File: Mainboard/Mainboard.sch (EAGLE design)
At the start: 9 parts, among them J1 USB3076-XX-X_REVC, J2 640455-5, J3 640455-2, J4 640455-4, J5 640455-4, J6 SJ-3523-SMT-TR, J7 640455-2, J8 929850-01-06-RB

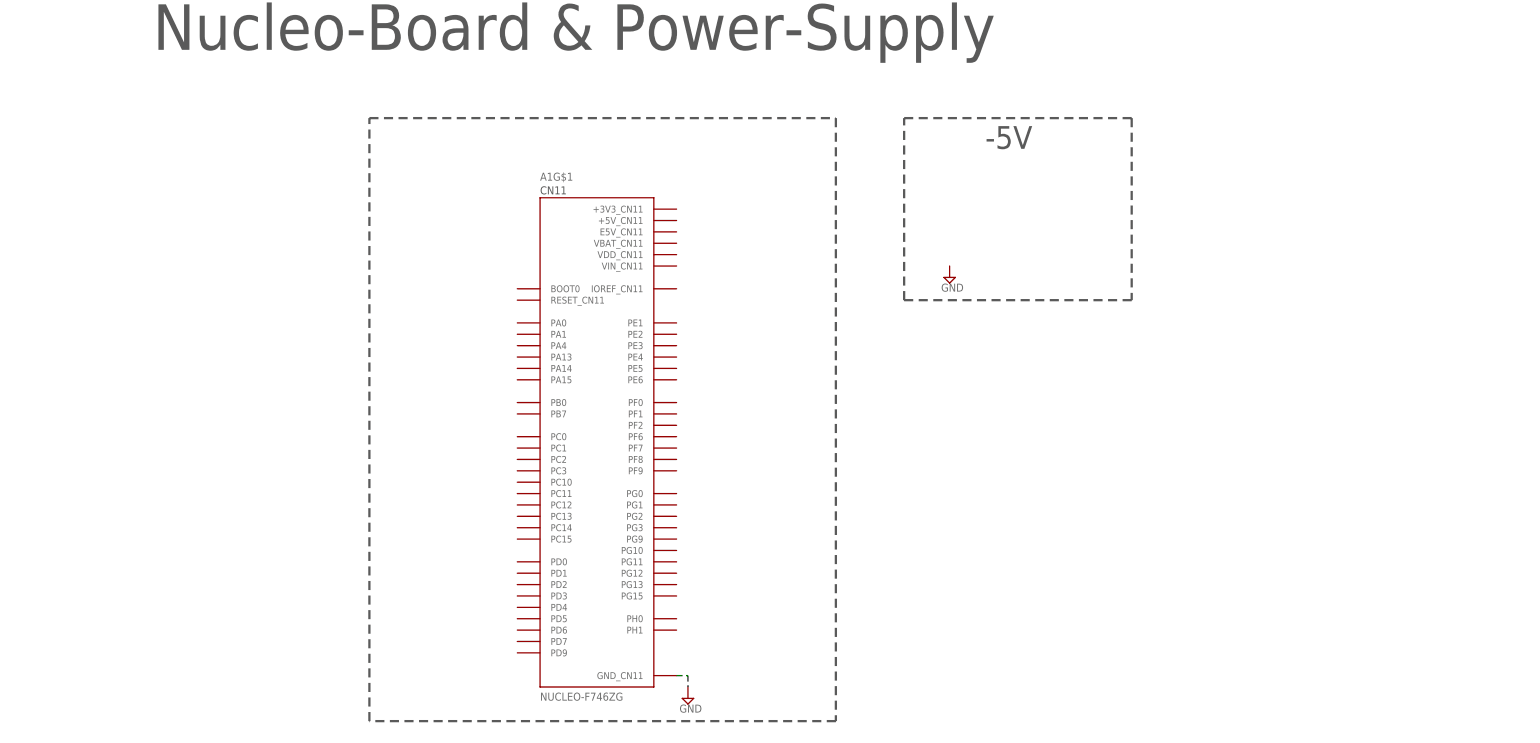
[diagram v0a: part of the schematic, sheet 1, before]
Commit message: Mainboard updated
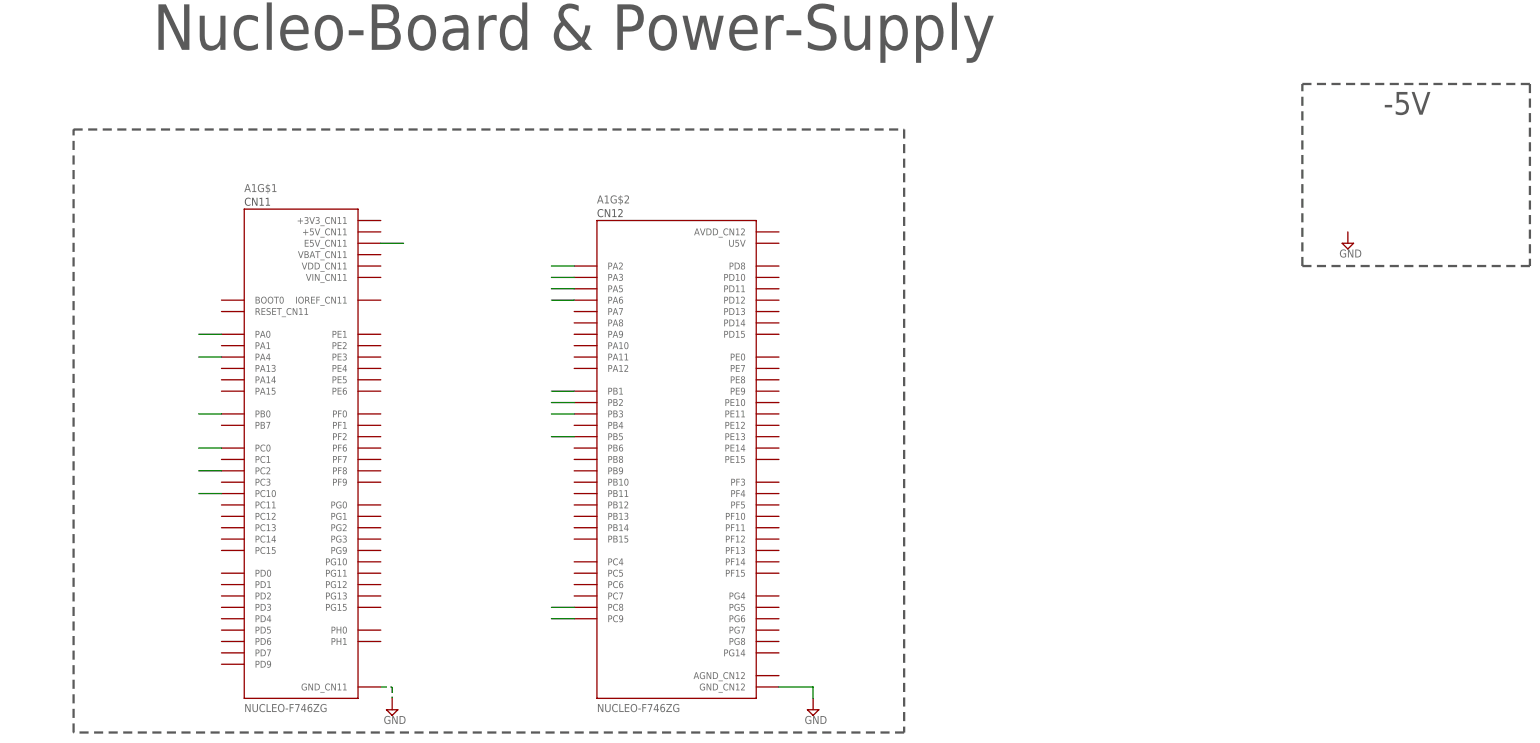
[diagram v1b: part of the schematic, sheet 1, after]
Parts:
- added C1, C2: 100n, rcl:C-EUC0603
- added C3, C4: 1u, rcl:C-EUC0603
- added IC1: TL072CD, SamacSys_Parts:TL072CD
- added IC2: LM386M-1_NOPB, SamacSys_Parts:LM386M-1_NOPB
- added J9: 61201421721, 61201421721:61201421721
- added R1, R9: 10k, rcl:R-EU_R0603
- added R10, R2, R3: 0, rcl:R-EU_R0603
- added R4: NP_0, rcl:R-EU_R0603
- added R5: 4k7, rcl:R-EU_R0603
- added R6: 15k, rcl:R-EU_R0603
- added R7: 33k, rcl:R-EU_R0603
- added R8: 100, rcl:R-EU_R0603
- added TS53YL104MR10: 100k, SamacSys_Parts:TS53YL203MR10
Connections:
- new net +3V3: J9.8
- new net 1_IN+: C3.2, IC1.1IN+, R1.2, R5.1
- new net 1_IN-: IC1.1IN-, R2.1
- new net 1_OUT: C3.1, IC1.1OUT, R3.1
- new net 2_IN-: IC1.2IN-, R6.2, R7.1
- new net 2_OUT: IC1.2OUT, R7.2, R8.1
- new net ADC_POTI: J9.9
- new net BUTTON_BACK: J9.13
- new net BUTTON_ENTER: J9.14
- new net DAC_OUT1: R10.1
- new net DISP_BUSY: J9.1
- new net DISP_CLK: J9.5
- new net DISP_CS: J9.4
- new net DISP_DC: J9.3
- new net DISP_DIN: J9.6
- new net DISP_RST: J9.2
- new net JOYSTICK_SW: J9.10
- new net JOYSTICK_VRX: J9.11
- new net JOYSTICK_VRY: J9.12
- new net N$1: A1G$1.E5V_CN11
- new net N$10: A1G$2.PB2
- new net N$11: A1G$2.PB3
- new net N$12: A1G$2.PB5
- new net N$13: A1G$1.PC0
- new net N$14: A1G$1.PC2
- new net N$15: A1G$2.PC8
- new net N$16: A1G$2.PC9
- new net N$17: A1G$1.PC10
- new net N$18: R10.2
- new net N$19: R2.2, R3.2, R4.1
- new net N$2: A1G$1.PA0
- new net N$20: R5.2, TS53YL104MR10.A
- new net N$21: R6.1, TS53YL104MR10.B
- new net N$22: C4.1, R8.2
- new net N$3: A1G$2.PA2
- new net N$4: A1G$2.PA3
- new net N$5: A1G$1.PA4
- new net N$6: A1G$2.PA5
- new net N$7: A1G$2.PA6
- new net N$8: A1G$1.PB0
- new net N$9: A1G$2.PB1
- net +5V: now also C2.2, IC1.VCC+
- net -5V: now also C1.2, IC1.VCC-
- net GND: now also A1G$2.GND_CN12, C1.1, C2.1, IC1.2IN+, J9.7, R1.1, R4.2, R9.1, TS53YL104MR10.C
- net PREAMP_AUDIO_OUT: now also C4.2, R9.2
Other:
- note added: "Adjustable Low Noise Preamplifier"
- note added: "Buffer / Non-Inverting Amp & Low Noise Preamplifier (for Headphones)"
- note added: "Buffer / Noninverting Amp."
- note added: "Highpass (DC-Filtering @ 16Hz)"
- note added: "IC Symbol & Power Supply Buffering"
- moved on the sheet: A1G$1

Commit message: Mainboard updated II
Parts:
- added C10, C7: 1m, rcl:CPOL-EUE2.5-5
- added C11: 1u, rcl:C-EUC0603
- added C5, C6: 100u, rcl:CPOL-EUE2.5-5
- added C8: 100n, rcl:C-EUC0603
- added C9: NP_10u, rcl:C-EUC0603
- added R11: NP_1k2, rcl:R-EU_R0603
- added R12, R13: 0, rcl:R-EU_R0603
- added R14: 10k, rcl:R-EU_R0603
- added TS53YL104MR1: 10k, SamacSys_Parts:TS53YL203MR10
- J3: value 640455-2 -> 640455-3; device 640455-2:640455-2 -> 640455-3:640455-3
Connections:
- net N$3 renamed USART2_TX
- net N$4 renamed USART2_RX
- removed net N$10: A1G$2.PB2
- removed net N$11: A1G$2.PB3
- removed net N$12: A1G$2.PB5
- removed net N$13: A1G$1.PC0
- removed net N$14: A1G$1.PC2
- removed net N$15: A1G$2.PC8
- removed net N$16: A1G$2.PC9
- removed net N$17: A1G$1.PC10
- removed net N$2: A1G$1.PA0
- removed net N$5: A1G$1.PA4
- removed net N$6: A1G$2.PA5
- removed net N$7: A1G$2.PA6
- removed net N$8: A1G$1.PB0
- removed net N$9: A1G$2.PB1
- new net ADC_EMG_AC: A1G$1.PF7
- new net ADC_EMG_DC: A1G$1.PF6
- new net ADC_KEYS: A1G$1.PC2, C11.1, R14.2
- new net DAC_OUT2: A1G$2.PA5, R13.1
- new net GYRO_I2C_SCL: A1G$1.PF1
- new net GYRO_I2C_SDA: A1G$1.PF0
- new net N$23: IC2.GAIN_1, R11.1
- new net N$24: IC2.+INPUT, TS53YL104MR1.B
- new net N$25: C9.1, R11.2
- new net N$26: C9.2, IC2.GAIN_2
- new net N$27: R12.2, TS53YL104MR1.A
- new net N$28: C5.+, IC2.BYPASS
- new net N$29: C7.+, C8.1, IC2.VOUT
- new net USART3_RX: A1G$1.PD9
- new net USART3_TX: A1G$2.PD8
- net +5V: now also A1G$1.E5V_CN11, C10.+, C6.+, IC2.VS
- net 1_OUT: now also R12.1
- net ADC_POTI: now also A1G$1.PC0
- net BUTTON_BACK: now also A1G$2.PC9
- net BUTTON_ENTER: now also A1G$2.PE8
- net DAC_OUT1: now also A1G$1.PA4
- net DISP_BUSY: now also A1G$2.PB1
- net DISP_CLK: now also A1G$2.PB3
- net DISP_CS: now also A1G$2.PC8
- net DISP_DC: now also A1G$1.PA0
- net DISP_DIN: now also A1G$2.PB5
- net DISP_RST: now also A1G$2.PF12
- net GND: now also C10.-, C11.2, C5.-, C6.-, C8.2, IC2.-INPUT, IC2.GND, TS53YL104MR1.C
- net JOYSTICK_SW: now also A1G$1.PG0
- net JOYSTICK_VRX: now also A1G$2.PA6
- net JOYSTICK_VRY: now also A1G$1.PB0
- net N$1: now also J3.3, R14.1; no longer A1G$1.E5V_CN11
- net N$18: now also R13.2
- net POWERAMP_AUDIO_OUT: now also C7.-
- net SD_CLK: now also A1G$1.PC10
- net SD_CS: now also A1G$2.PF10
- net SD_DI: now also A1G$2.PB2
- net SD_DO: now also A1G$1.PC11
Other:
- note added: "E5V is used as power source when JP3 is set and JP1 is not set."
- note added: "LM386 Power Amplifier"
- note added: "MOSI"
- moved on the sheet: C1, C2, C3, C4, IC1, IC2, J1, J6, J7, J9, R1, R10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

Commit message: # Mainboard updated
# Keyboard V2:

	# Bug fixed (lowest Pad not GND)
	# 1 more key (upper C)
	# PEACE sign corrected

# General cleanup
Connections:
- net JOYSTICK_VRX renamed ADC_JOYSTICK_VRX
- net JOYSTICK_VRY renamed ADC_JOYSTICK_VRY
- removed net AC_OUT: J2.2
- removed net DC_OUT: J2.3
- removed net GYRO_SCL: J5.2
- removed net GYRO_SDA: J5.1
- removed net UC_AUDIO_OUT: J4.4
- net +3V3: now also A1G$1.+3V3_CN11, J3.2
- net 3V3: no longer J3.2
- net ADC_EMG_AC: now also J2.2
- net ADC_EMG_DC: now also J2.3
- net DAC_OUT1: now also J4.4
- net GND: now also A1G$3.GND_CN8, A1G$4.GND_CN9, A1G$5.GND_CN7, A1G$6.AGND_CN10, A1G$6.GND_CN10
- net GYRO_I2C_SCL: now also J5.2
- net GYRO_I2C_SDA: now also J5.1
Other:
- note added: "Misc"
- moved on the sheet: A1G$1, A1G$2, A1G$3, A1G$4, A1G$5, A1G$6, C10, J1, J2, J4, J5, J8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

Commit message: Mainboard updated IV
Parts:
- added C12: 4u7, rcl:C-EUC0603
- added C13, C14: 22u, rcl:C-EUC0603
- added R15, R16: 100k, rcl:R-EU_R0603
- added R17, R18, R19: 1Meg, rcl:R-EU_R0603
- added U1: MAX889RESA, MAX889RESA:MAX889RESA
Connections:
- new net N$3: R15.1, R16.2, U1.FB
- new net N$5: C12.2, U1.CAP+
- new net N$6: C12.1, U1.CAP-
- net +5V: now also C14.2, R16.1, U1.!SHDN, U1.IN
- net -5V: now also C13.2, R15.2, U1.OUT
- net ADC_JOYSTICK_VRX: now also R19.2
- net ADC_JOYSTICK_VRY: now also R18.2
- net ADC_POTI: now also R17.2
- net GND: now also C13.1, C14.1, R17.1, R18.1, R19.1, U1.AGND, U1.GND
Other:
- note added: "Anti-floating PDs"
- note added: "Nucleo-Board"
- note added: "Power Supply: -5V"
- note removed: "-5V"
- note removed: "Nucleo-Board & Power-Supply"
- moved on the sheet: A1G$1, A1G$2, A1G$3, A1G$4, A1G$5, A1G$6, J7, J9

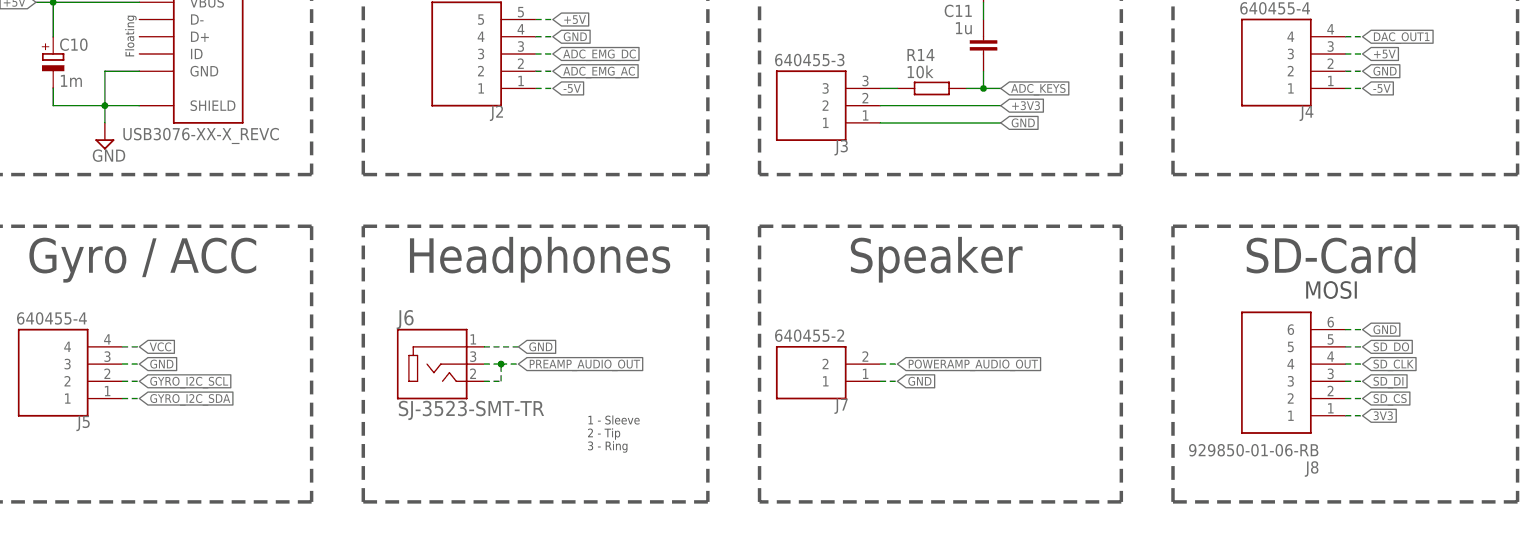
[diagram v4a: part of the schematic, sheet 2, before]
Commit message: # Mainboard updated V
# Keys finalizing production
# EQ finalizing production
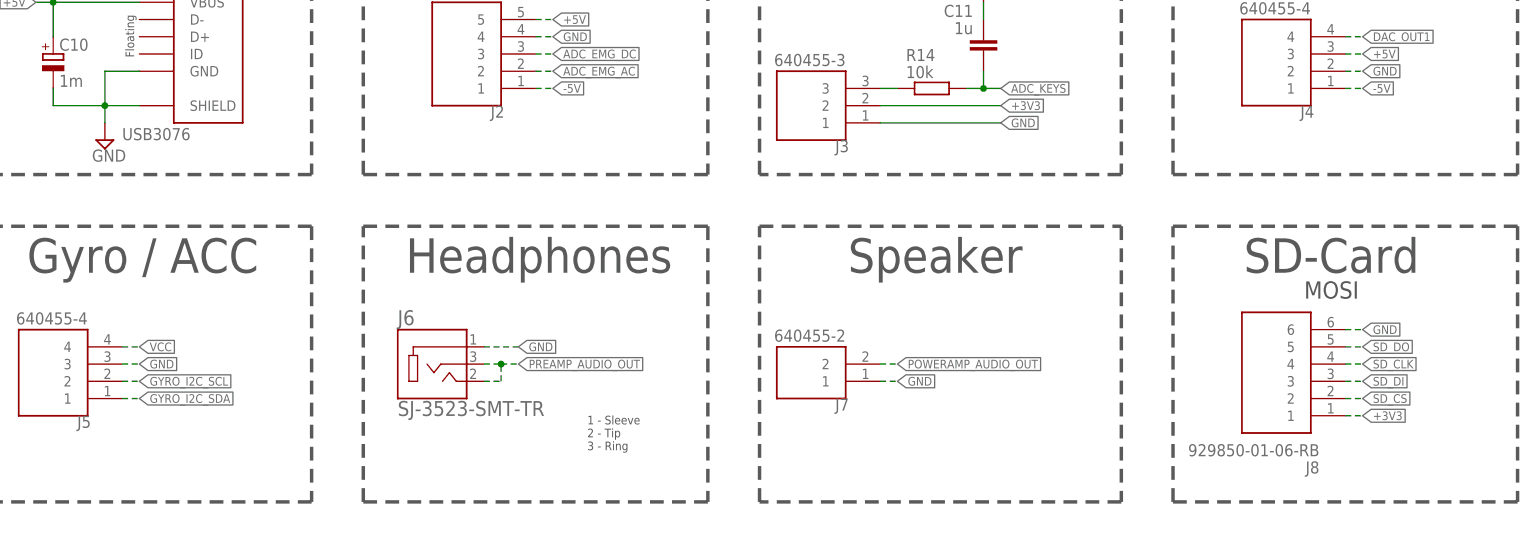
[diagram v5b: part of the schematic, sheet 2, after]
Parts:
- J1: value USB3076-XX-X_REVC -> USB3076
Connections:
- removed net 3V3: J8.1
- net +3V3: now also J8.1
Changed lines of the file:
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@@
 <setting verticaltext="up"/>
 </settings>
-<grid distance="0.1" unitdist="inch" unit="inch" style="lines" multiple="1" display="yes" altdistance="0.01" altunitdist="inch" altunit="inch"/>
+<grid distance="0.1" unitdist="inch" unit="inch" style="lines" multiple="1" display="no" altdistance="0.01" altunitdist="inch" altunit="inch"/>
 <layers>
 <layer number="1" name="Top" color="4" fill="1" visible="no" active="no"/>
@@
 <layer number="97" name="Info" color="7" fill="1" visible="yes" active="yes"/>
 <layer number="98" name="Guide" color="6" fill="1" visible="yes" active="yes"/>
+<layer number="100" name="PRINT" color="7" fill="1" visible="yes" active="yes"/>
 </layers>
 <schematic xreflabel="%F%N/%S.%C%R" xrefpart="/%S.%C%R">
@@
 <parts>
 <part name="A1" library="NUCLEO-F746ZG" deviceset="NUCLEO-F746ZG" device=""/>
-<part name="J1" library="USB3076-XX-X_REVC" deviceset="USB3076-XX-X_REVC" device=""/>
+<part name="J1" library="USB3076-XX-X_REVC" deviceset="USB3076-XX-X_REVC" device="" value="USB3076"/>
 <part name="SUPPLY1" library="supply2" deviceset="GND" device=""/>
 <part name="FRAME2" library="frames" deviceset="FRAME_A_L" device=""/>
@@
 </segment>
 </net>
-<net name="3V3" class="0">
-<segment>
-<pinref part="J8" gate="G$1" pin="1"/>
-<wire x1="91.44" y1="20.32" x2="93.98" y2="20.32" width="0.1524" layer="91" style="longdash"/>
-<label x="93.98" y="20.32" size="1.27" layer="95" xref="yes"/>
-</segment>
-</net>
 <net name="DAC_OUT1" class="0">
 <segment>
@@
 <label x="40.64" y="66.04" size="1.27" layer="95" xref="yes"/>
 </segment>
-</net>
+<segment>
+<pinref part="J8" gate="G$1" pin="1"/>
+<wire x1="91.44" y1="20.32" x2="93.98" y2="20.32" width="0.1524" layer="91" style="longdash"/>
+<label x="93.98" y="20.32" size="1.27" layer="95" xref="yes"/>
+</segment>
+</net>

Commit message: Mainboard updated VI (ready2route)
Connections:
- removed net N$18: R10.2, R13.2
- new net N$2: C3.2, R1.2, R5.1
- net 1_IN+: now also R10.2, R13.2; no longer C3.2, R1.2, R5.1
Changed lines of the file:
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@@
 </segment>
 <segment>
+<pinref part="R10" gate="G$1" pin="2"/>
+<wire x1="-91.44" y1="2.54" x2="-96.52" y2="2.54" width="0.1524" layer="91"/>
+<wire x1="-96.52" y1="2.54" x2="-96.52" y2="7.62" width="0.1524" layer="91"/>
+<wire x1="-96.52" y1="7.62" x2="-99.06" y2="7.62" width="0.1524" layer="91"/>
+<pinref part="R13" gate="G$1" pin="2"/>
+<wire x1="-99.06" y1="2.54" x2="-96.52" y2="2.54" width="0.1524" layer="91"/>
+<junction x="-96.52" y="2.54"/>
 <label x="-91.44" y="2.54" size="1.27" layer="95" xref="yes"/>
-<pinref part="C3" gate="G$1" pin="2"/>
-<wire x1="-58.42" y1="0" x2="-53.34" y2="0" width="0.1524" layer="91"/>
-<pinref part="R1" gate="G$1" pin="2"/>
-<wire x1="-53.34" y1="-12.7" x2="-53.34" y2="0" width="0.1524" layer="91"/>
-<pinref part="R5" gate="G$1" pin="1"/>
-<wire x1="-53.34" y1="0" x2="-40.64" y2="0" width="0.1524" layer="91"/>
-<junction x="-53.34" y="0"/>
 </segment>
 </net>
@@
 </segment>
 </net>
-<net name="N$18" class="0">
-<segment>
-<pinref part="R10" gate="G$1" pin="2"/>
-<wire x1="-91.44" y1="2.54" x2="-96.52" y2="2.54" width="0.1524" layer="91"/>
-<wire x1="-96.52" y1="2.54" x2="-96.52" y2="7.62" width="0.1524" layer="91"/>
-<wire x1="-96.52" y1="7.62" x2="-99.06" y2="7.62" width="0.1524" layer="91"/>
-<pinref part="R13" gate="G$1" pin="2"/>
-<wire x1="-99.06" y1="2.54" x2="-96.52" y2="2.54" width="0.1524" layer="91"/>
-<junction x="-96.52" y="2.54"/>
-</segment>
-</net>
 <net name="DAC_OUT1" class="0">
 <segment>
@@
 </segment>
 </net>
+<net name="N$2" class="0">
+<segment>
+<pinref part="C3" gate="G$1" pin="2"/>
+<pinref part="R5" gate="G$1" pin="1"/>
+<wire x1="-58.42" y1="0" x2="-53.34" y2="0" width="0.1524" layer="91"/>
+<pinref part="R1" gate="G$1" pin="2"/>
+<wire x1="-53.34" y1="0" x2="-40.64" y2="0" width="0.1524" layer="91"/>
+<wire x1="-53.34" y1="-12.7" x2="-53.34" y2="0" width="0.1524" layer="91"/>
+<junction x="-53.34" y="0"/>
+</segment>
+</net>

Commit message: Mainboard updated VII
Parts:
- added C15, C16, C17, C18, C19, C20, C21, C22, C23, C24: 1u, rcl:C-EUC0603
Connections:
- removed net VCC: J5.4
- net +3V3: now also C19.2, C20.2, C21.2, C22.2, J5.4
- net +5V: now also C15.2, C16.2, C17.2, C18.2
- net -5V: now also C23.2, C24.2
- net GND: now also C15.1, C16.1, C17.1, C18.1, C19.1, C20.1, C21.1, C22.1, C23.1, C24.1
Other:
- note added: "+3V3 Buffering"
- note added: "+5V Buffering"
- note added: "-5V Buffering"
- moved on the sheet: C10, J1, R17, R18, R19
